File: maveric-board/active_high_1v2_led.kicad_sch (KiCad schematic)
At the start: 4 parts, among them Q1 DMN2005K-7

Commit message: some few notes
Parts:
- R14: value R_US -> 100R; JLCPCB Part # (none) -> C25076
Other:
- note added: "Vgs, max = 0.9V @ Id = 100uA, Vds = Vgs Cin = 36pF"
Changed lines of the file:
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@@
+		)
+	)
+	(text "Vgs, max = 0.9V @ Id = 100uA, Vds = Vgs\nCin = 36pF"
+		(exclude_from_sim no)
+		(at 85.598 52.07 0)
+		(effects
+			(font
+				(size 1.27 1.27)
+			)
 		)
 	)
@@
 			)
 		)
-		(property "Value" "R_US"
+		(property "Value" "100R"
 			(at 48.26 31.7499 0)
 			(effects
@@
 			)
 		)
-		(property "Description" "Resistor, US symbol"
+		(property "Description" "0402WGF1000TCE"
 			(at 45.72 30.48 0)
 			(effects
+				(font
+					(size 1.27 1.27)
+				)
+				(hide yes)
+			)
+		)
+		(property "JLCPCB Part #" "C25076"
+			(at 45.72 30.48 0)
+			(effects

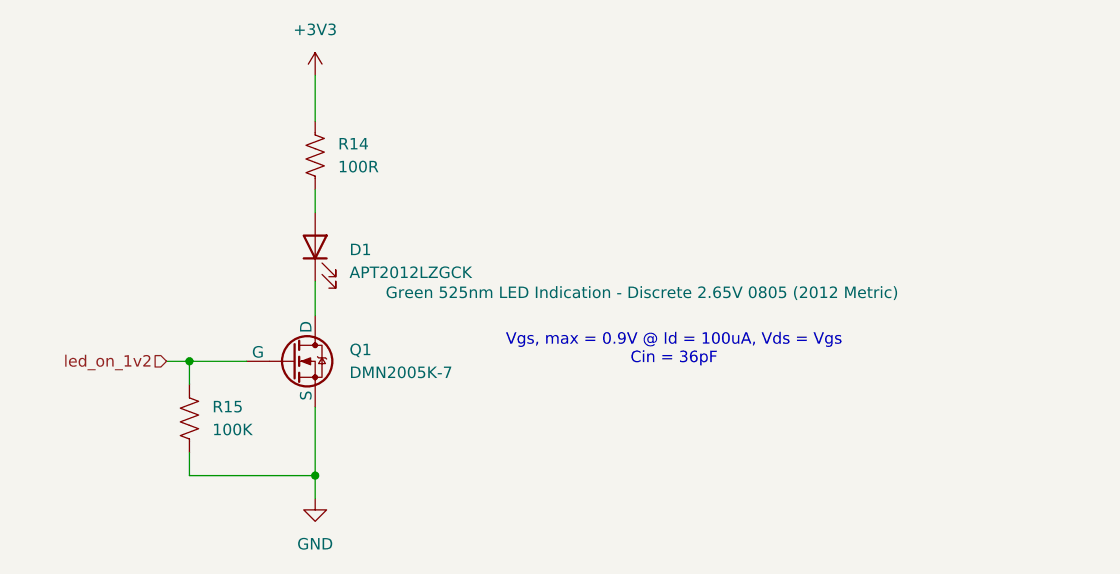
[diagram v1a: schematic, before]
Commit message: wire up the LEDs
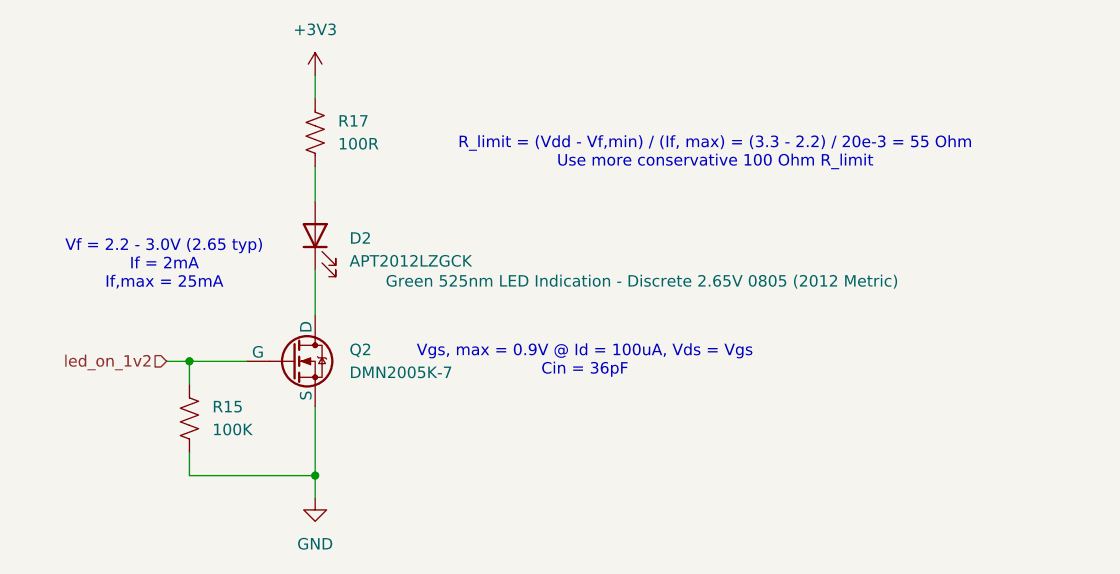
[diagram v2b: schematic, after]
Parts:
- renumbered D1 to D2, Q1 to Q2, R14 to R17
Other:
- note added: "R_limit = (Vdd - Vf,min) / (If, max) = (3.3 - 2.2) / 20e-3 = 55 Ohm Use more conservative 100 Ohm R_limit"
- note added: "Vf = 2.2 - 3.0V (2.65 typ) If = 2mA If,max = 25mA"
- moved on the sheet: D2, R17
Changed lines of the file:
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@@
-	(wire
-		(pts
-			(xy 45.72 34.29) (xy 45.72 36.83)
-		)
-		(stroke
-			(width 0)
-			(type default)
-		)
-	)
 	(wire
 		(pts
@@
 	(wire
 		(pts
-			(xy 45.72 44.45) (xy 45.72 48.26)
+			(xy 45.72 43.18) (xy 45.72 48.26)
 		)
 		(stroke
@@
 	(wire
 		(pts
-			(xy 45.72 21.59) (xy 45.72 26.67)
+			(xy 45.72 21.59) (xy 45.72 24.13)
+		)
+		(stroke
+			(width 0)
+			(type default)
+		)
+	)
+	(wire
+		(pts
+			(xy 45.72 31.75) (xy 45.72 35.56)
 		)
 		(stroke
@@
 		)
 	)
+	(text "Vf = 2.2 - 3.0V (2.65 typ)\nIf = 2mA\nIf,max = 25mA"
+		(exclude_from_sim no)
+		(at 28.956 42.672 0)
+		(effects
+			(font
+				(size 1.27 1.27)
+			)
+		)
+	)
+	(text "R_limit = (Vdd - Vf,min) / (If, max) = (3.3 - 2.2) / 20e-3 = 55 Ohm\nUse more conservative 100 Ohm R_limit"
+		(exclude_from_sim no)
+		(at 90.17 30.226 0)
+		(effects
+			(font
+				(size 1.27 1.27)
+			)
+		)
+	)
 	(text "Vgs, max = 0.9V @ Id = 100uA, Vds = Vgs\nCin = 36pF"
 		(exclude_from_sim no)
-		(at 85.598 52.07 0)
+		(at 75.692 53.34 0)
 		(effects
 			(font
@@
 		(dnp no)
 		(fields_autoplaced yes)
-		(property "Reference" "#PWR068"
+		(property "Reference" "#PWR091"
 			(at 45.72 74.93 0)
 			(effects
@@
 		)
 		(instances
-			(project ""
+			(project "maveric-board"
+				(path "/ae861d46-65fb-4872-932f-ad48addb0154/04d5a329-5af7-4fa0-b263-ed8b9ef94f0b"
+					(reference "#PWR091")
+					(unit 1)
+				)
+				(path "/ae861d46-65fb-4872-932f-ad48addb0154/07de628d-3b41-4acd-98a7-6b7c73c5b4dd"
+					(reference "#PWR093")
+					(unit 1)
+				)
+				(path "/ae861d46-65fb-4872-932f-ad48addb0154/482467b2-b94e-4ec7-a3c4-312d002b6711"
+					(reference "#PWR095")
+					(unit 1)
+				)
 				(path "/ae861d46-65fb-4872-932f-ad48addb0154/9dce5c8c-15df-41df-971c-7c9355dface0"
 					(reference "#PWR068")
+					(unit 1)
+				)
+				(path "/ae861d46-65fb-4872-932f-ad48addb0154/d720b503-5d41-4e8c-a69b-3a22cbc341eb"
+					(reference "#PWR097")
 					(unit 1)
 				)
@@
 		(dnp no)
 		(fields_autoplaced yes)
-		(property "Reference" "Q1"
+		(property "Reference" "Q2"
 			(at 49.53 52.0699 0)
 			(effects
@@
 		)
 		(instances
-			(project ""
-				(path "/ae861d46-65fb-4872-932f-ad48addb0154/9dce5c8c-15df-41df-971c-7c9355dface0"
-					(reference "Q1")
+			(project "maveric-board"
+				(path "/ae861d46-65fb-4872-932f-ad48addb0154/04d5a329-5af7-4fa0-b263-ed8b9ef94f0b"
+					(reference "Q2")
+					(unit 1)
+				)
+				(path "/ae861d46-65fb-4872-932f-ad48addb0154/07de628d-3b41-4acd-98a7-6b7c73c5b4dd"
+					(reference "Q3")
+					(unit 1)
+				)
+				(path "/ae861d46-65fb-4872-932f-ad48addb0154/482467b2-b94e-4ec7-a3c4-312d002b6711"
+					(reference "Q4")
+					(unit 1)
+				)
+				(path "/ae861d46-65fb-4872-932f-ad48addb0154/d720b503-5d41-4e8c-a69b-3a22cbc341eb"
+					(reference "Q5")
 					(unit 1)
 				)
@@
 	(symbol
 		(lib_id "Device:R_US")
-		(at 45.72 30.48 0)
+		(at 45.72 27.94 0)
 		(unit 1)
 		(exclude_from_sim no)
@@
 		(dnp no)
 		(fields_autoplaced yes)
-		(property "Reference" "R14"
+		(property "Reference" "R17"
+			(at 48.26 26.6699 0)
+			(effects
+				(font
+					(size 1.27 1.27)
+				)
+				(justify left)
+			)
+		)
+		(property "Value" "100R"
 			(at 48.26 29.2099 0)
 			(effects
@@
 			)
 		)
-		(property "Value" "100R"
-			(at 48.26 31.7499 0)
-			(effects
-				(font
-					(size 1.27 1.27)
-				)
-				(justify left)
-			)
-		)
 		(property "Footprint" ""
-			(at 46.736 30.734 90)
+			(at 46.736 28.194 90)
 			(effects
 				(font
@@
 		)
 		(property "Datasheet" "~"
-			(at 45.72 30.48 0)
+			(at 45.72 27.94 0)
 			(effects
 				(font
@@
 		)
 		(property "Description" "0402WGF1000TCE"
-			(at 45.72 30.48 0)
+			(at 45.72 27.94 0)
 			(effects
 				(font
@@
 		)
 		(property "JLCPCB Part #" "C25076"
-			(at 45.72 30.48 0)
+			(at 45.72 27.94 0)
 			(effects
 				(font
@@
 		)
 		(instances
-			(project ""
-				(path "/ae861d46-65fb-4872-932f-ad48addb0154/9dce5c8c-15df-41df-971c-7c9355dface0"
-					(reference "R14")
+			(project "maveric-board"
+				(path "/ae861d46-65fb-4872-932f-ad48addb0154/04d5a329-5af7-4fa0-b263-ed8b9ef94f0b"
+					(reference "R17")
+					(unit 1)
+				)
+				(path "/ae861d46-65fb-4872-932f-ad48addb0154/07de628d-3b41-4acd-98a7-6b7c73c5b4dd"
+					(reference "R19")
+					(unit 1)
+				)
+				(path "/ae861d46-65fb-4872-932f-ad48addb0154/482467b2-b94e-4ec7-a3c4-312d002b6711"
+					(reference "R21")
+					(unit 1)
+				)
+				(path "/ae861d46-65fb-4872-932f-ad48addb0154/d720b503-5d41-4e8c-a69b-3a22cbc341eb"
+					(reference "R23")
 					(unit 1)
 				)
@@
 		(instances
 			(project "maveric-board"
+				(path "/ae861d46-65fb-4872-932f-ad48addb0154/04d5a329-5af7-4fa0-b263-ed8b9ef94f0b"
+					(reference "R16")
+					(unit 1)
+				)
+				(path "/ae861d46-65fb-4872-932f-ad48addb0154/07de628d-3b41-4acd-98a7-6b7c73c5b4dd"
+					(reference "R18")
+					(unit 1)
+				)
+				(path "/ae861d46-65fb-4872-932f-ad48addb0154/482467b2-b94e-4ec7-a3c4-312d002b6711"
+					(reference "R20")
+					(unit 1)
+				)
 				(path "/ae861d46-65fb-4872-932f-ad48addb0154/9dce5c8c-15df-41df-971c-7c9355dface0"
 					(reference "R15")
 					(unit 1)
 				)
+				(path "/ae861d46-65fb-4872-932f-ad48addb0154/d720b503-5d41-4e8c-a69b-3a22cbc341eb"
+					(reference "R22")
+					(unit 1)
+				)
 			)
 		)
@@
 	(symbol
 		(lib_id "Device:LED")
-		(at 45.72 40.64 90)
+		(at 45.72 39.37 90)
 		(unit 1)
 		(exclude_from_sim no)
@@
 		(on_board yes)
 		(dnp no)
-		(property "Reference" "D1"
-			(at 49.53 40.9574 90)
+		(property "Reference" "D2"
+			(at 49.53 39.6874 90)
 			(effects
 				(font
@@
 		)
 		(property "Value" "APT2012LZGCK"
-			(at 49.53 43.4974 90)
+			(at 49.53 42.2274 90)
 			(effects
 				(font
@@
 		)
 		(property "Footprint" "maveric-parts:APT2012LZGCK"
-			(at 45.72 40.64 0)
+			(at 45.72 39.37 0)
 			(effects
 				(font
@@
 		)
 		(property "Datasheet" "~"
-			(at 45.72 40.64 0)
+			(at 45.72 39.37 0)
 			(effects
 				(font
@@
 		)
 		(property "Description" "Green 525nm LED Indication - Discrete 2.65V 0805 (2012 Metric)"
-			(at 82.042 45.72 90)
+			(at 82.042 44.45 90)
 			(effects
 				(font
@@
 		)
 		(property "JLCPCB Part #" "C5569446"
-			(at 45.72 40.64 90)
+			(at 45.72 39.37 90)
 			(effects
 				(font
@@
 		)
 		(instances
-			(project ""
-				(path "/ae861d46-65fb-4872-932f-ad48addb0154/9dce5c8c-15df-41df-971c-7c9355dface0"
-					(reference "D1")
+			(project "maveric-board"
+				(path "/ae861d46-65fb-4872-932f-ad48addb0154/04d5a329-5af7-4fa0-b263-ed8b9ef94f0b"
+					(reference "D2")
+					(unit 1)
+				)
+				(path "/ae861d46-65fb-4872-932f-ad48addb0154/07de628d-3b41-4acd-98a7-6b7c73c5b4dd"
+					(reference "D3")
+					(unit 1)
+				)
+				(path "/ae861d46-65fb-4872-932f-ad48addb0154/482467b2-b94e-4ec7-a3c4-312d002b6711"
+					(reference "D4")
+					(unit 1)
+				)
+				(path "/ae861d46-65fb-4872-932f-ad48addb0154/d720b503-5d41-4e8c-a69b-3a22cbc341eb"
+					(reference "D5")
 					(unit 1)
 				)
@@
 		(dnp no)
 		(fields_autoplaced yes)
-		(property "Reference" "#PWR066"
+		(property "Reference" "#PWR069"
 			(at 45.72 25.4 0)
 			(effects
@@
 		)
 		(instances
-			(project ""
+			(project "maveric-board"
+				(path "/ae861d46-65fb-4872-932f-ad48addb0154/04d5a329-5af7-4fa0-b263-ed8b9ef94f0b"
+					(reference "#PWR069")
+					(unit 1)
+				)
+				(path "/ae861d46-65fb-4872-932f-ad48addb0154/07de628d-3b41-4acd-98a7-6b7c73c5b4dd"
+					(reference "#PWR092")
+					(unit 1)
+				)
+				(path "/ae861d46-65fb-4872-932f-ad48addb0154/482467b2-b94e-4ec7-a3c4-312d002b6711"
+					(reference "#PWR094")
+					(unit 1)
+				)
 				(path "/ae861d46-65fb-4872-932f-ad48addb0154/9dce5c8c-15df-41df-971c-7c9355dface0"
 					(reference "#PWR066")
 					(unit 1)
 				)
+				(path "/ae861d46-65fb-4872-932f-ad48addb0154/d720b503-5d41-4e8c-a69b-3a22cbc341eb"
+					(reference "#PWR096")
+					(unit 1)
+				)

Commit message: add clocking notes
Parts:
- renumbered R15 to R16
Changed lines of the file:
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@@
 		(dnp no)
 		(fields_autoplaced yes)
-		(property "Reference" "R15"
+		(property "Reference" "R16"
 			(at 34.29 58.4199 0)
 			(effects

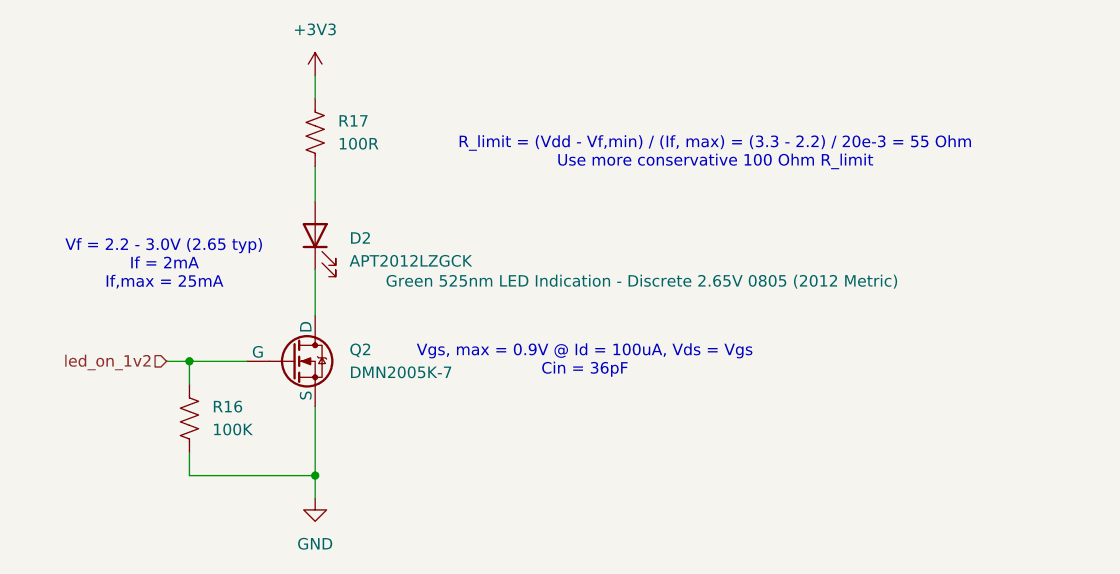
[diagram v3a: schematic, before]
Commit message: reannotate, fix all ERCs
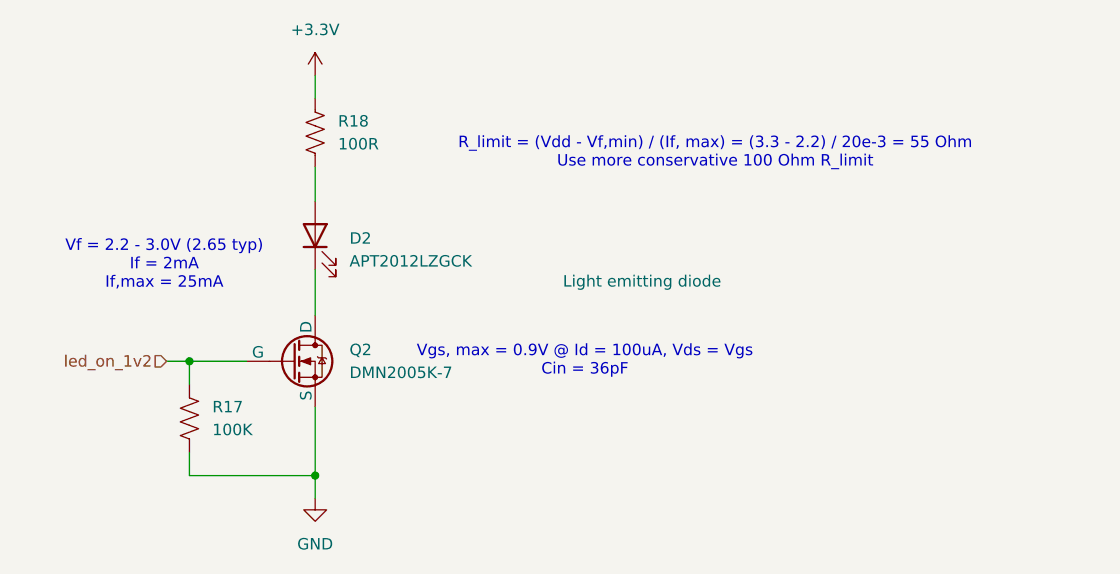
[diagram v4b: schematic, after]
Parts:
- renumbered R16 to R17, R17 to R18
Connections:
- net +3V3 renamed +3.3V
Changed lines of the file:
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@@
 		(dnp no)
 		(fields_autoplaced yes)
-		(property "Reference" "#PWR091"
+		(property "Reference" "#PWR095"
 			(at 45.72 74.93 0)
 			(effects
@@
 			(project "maveric-board"
 				(path "/ae861d46-65fb-4872-932f-ad48addb0154/04d5a329-5af7-4fa0-b263-ed8b9ef94f0b"
-					(reference "#PWR091")
+					(reference "#PWR095")
 					(unit 1)
 				)
 				(path "/ae861d46-65fb-4872-932f-ad48addb0154/07de628d-3b41-4acd-98a7-6b7c73c5b4dd"
+					(reference "#PWR097")
+					(unit 1)
+				)
+				(path "/ae861d46-65fb-4872-932f-ad48addb0154/482467b2-b94e-4ec7-a3c4-312d002b6711"
+					(reference "#PWR099")
+					(unit 1)
+				)
+				(path "/ae861d46-65fb-4872-932f-ad48addb0154/9dce5c8c-15df-41df-971c-7c9355dface0"
 					(reference "#PWR093")
 					(unit 1)
 				)
-				(path "/ae861d46-65fb-4872-932f-ad48addb0154/482467b2-b94e-4ec7-a3c4-312d002b6711"
-					(reference "#PWR095")
-					(unit 1)
-				)
-				(path "/ae861d46-65fb-4872-932f-ad48addb0154/9dce5c8c-15df-41df-971c-7c9355dface0"
-					(reference "#PWR068")
-					(unit 1)
-				)
 				(path "/ae861d46-65fb-4872-932f-ad48addb0154/d720b503-5d41-4e8c-a69b-3a22cbc341eb"
-					(reference "#PWR097")
+					(reference "#PWR0101")
 					(unit 1)
 				)
@@
 			)
 		)
-		(property "Datasheet" ""
+		(property "Datasheet" "https://ngspice.sourceforge.io/docs/ngspice-html-manual/manual.xhtml#cha_MOSFETs"
 			(at 43.18 66.04 0)
 			(effects
@@
 			)
 		)
-		(property "Description" "MOSFET N-CH 20V 300MA SOT23-3"
+		(property "Description" "N-MOSFET transistor, drain/source/gate"
 			(at 43.18 53.34 0)
 			(effects
@@
 		(property "JLCPCB Part #" "C260950"
 			(at 43.18 53.34 0)
+			(effects
+				(font
+					(size 1.27 1.27)
+				)
+				(hide yes)
+			)
+		)
+		(property "Sim.Device" "NMOS"
+			(at 43.18 70.485 0)
+			(effects
+				(font
+					(size 1.27 1.27)
+				)
+				(hide yes)
+			)
+		)
+		(property "Sim.Type" "VDMOS"
+			(at 43.18 72.39 0)
+			(effects
+				(font
+					(size 1.27 1.27)
+				)
+				(hide yes)
+			)
+		)
+		(property "Sim.Pins" "1=D 2=G 3=S"
+			(at 43.18 68.58 0)
 			(effects
 				(font
@@
 				(path "/ae861d46-65fb-4872-932f-ad48addb0154/482467b2-b94e-4ec7-a3c4-312d002b6711"
 					(reference "Q4")
+					(unit 1)
+				)
+				(path "/ae861d46-65fb-4872-932f-ad48addb0154/9dce5c8c-15df-41df-971c-7c9355dface0"
+					(reference "Q1")
 					(unit 1)
 				)
@@
 		(dnp no)
 		(fields_autoplaced yes)
-		(property "Reference" "R17"
+		(property "Reference" "R18"
 			(at 48.26 26.6699 0)
 			(effects
@@
 			)
 		)
-		(property "Description" "0402WGF1000TCE"
+		(property "Description" "Resistor, US symbol"
 			(at 45.72 27.94 0)
 			(effects
@@
 			(project "maveric-board"
 				(path "/ae861d46-65fb-4872-932f-ad48addb0154/04d5a329-5af7-4fa0-b263-ed8b9ef94f0b"
-					(reference "R17")
+					(reference "R18")
 					(unit 1)
 				)
 				(path "/ae861d46-65fb-4872-932f-ad48addb0154/07de628d-3b41-4acd-98a7-6b7c73c5b4dd"
-					(reference "R19")
+					(reference "R20")
 					(unit 1)
 				)
 				(path "/ae861d46-65fb-4872-932f-ad48addb0154/482467b2-b94e-4ec7-a3c4-312d002b6711"
-					(reference "R21")
+					(reference "R22")
+					(unit 1)
+				)
+				(path "/ae861d46-65fb-4872-932f-ad48addb0154/9dce5c8c-15df-41df-971c-7c9355dface0"
+					(reference "R16")
 					(unit 1)
 				)
 				(path "/ae861d46-65fb-4872-932f-ad48addb0154/d720b503-5d41-4e8c-a69b-3a22cbc341eb"
-					(reference "R23")
+					(reference "R24")
+					(unit 1)
+				)
+			)
+		)
+	)
+	(symbol
+		(lib_id "power:+3.3V")
+		(at 45.72 21.59 0)
+		(unit 1)
+		(exclude_from_sim no)
+		(in_bom yes)
+		(on_board yes)
+		(dnp no)
+		(fields_autoplaced yes)
+		(property "Reference" "#PWR092"
+			(at 45.72 25.4 0)
+			(effects
+				(font
+					(size 1.27 1.27)
+				)
+				(hide yes)
+			)
+		)
+		(property "Value" "+3.3V"
+			(at 45.72 16.51 0)
+			(effects
+				(font
+					(size 1.27 1.27)
+				)
+			)
+		)
+		(property "Footprint" ""
+			(at 45.72 21.59 0)
+			(effects
+				(font
+					(size 1.27 1.27)
+				)
+				(hide yes)
+			)
+		)
+		(property "Datasheet" ""
+			(at 45.72 21.59 0)
+			(effects
+				(font
+					(size 1.27 1.27)
+				)
+				(hide yes)
+			)
+		)
+		(property "Description" "Power symbol creates a global label with name \"+3.3V\""
+			(at 45.72 21.59 0)
+			(effects
+				(font
+					(size 1.27 1.27)
+				)
+				(hide yes)
+			)
+		)
+		(pin "1"
+		)
+		(instances
+			(project ""
+				(path "/ae861d46-65fb-4872-932f-ad48addb0154/04d5a329-5af7-4fa0-b263-ed8b9ef94f0b"
+					(reference "#PWR092")
+					(unit 1)
+				)
+				(path "/ae861d46-65fb-4872-932f-ad48addb0154/07de628d-3b41-4acd-98a7-6b7c73c5b4dd"
+					(reference "#PWR094")
+					(unit 1)
+				)
+				(path "/ae861d46-65fb-4872-932f-ad48addb0154/482467b2-b94e-4ec7-a3c4-312d002b6711"
+					(reference "#PWR096")
+					(unit 1)
+				)
+				(path "/ae861d46-65fb-4872-932f-ad48addb0154/9dce5c8c-15df-41df-971c-7c9355dface0"
+					(reference "#PWR023")
+					(unit 1)
+				)
+				(path "/ae861d46-65fb-4872-932f-ad48addb0154/d720b503-5d41-4e8c-a69b-3a22cbc341eb"
+					(reference "#PWR098")
 					(unit 1)
 				)
@@
 		(dnp no)
 		(fields_autoplaced yes)
-		(property "Reference" "R16"
+		(property "Reference" "R17"
 			(at 34.29 58.4199 0)
 			(effects
@@
 			)
 		)
-		(property "Description" "0603WAF1003T5E"
+		(property "Description" "Resistor, US symbol"
 			(at 31.75 59.69 0)
 			(effects
@@
 			(project "maveric-board"
 				(path "/ae861d46-65fb-4872-932f-ad48addb0154/04d5a329-5af7-4fa0-b263-ed8b9ef94f0b"
-					(reference "R16")
+					(reference "R17")
 					(unit 1)
 				)
 				(path "/ae861d46-65fb-4872-932f-ad48addb0154/07de628d-3b41-4acd-98a7-6b7c73c5b4dd"
-					(reference "R18")
+					(reference "R19")
 					(unit 1)
 				)
 				(path "/ae861d46-65fb-4872-932f-ad48addb0154/482467b2-b94e-4ec7-a3c4-312d002b6711"
-					(reference "R20")
+					(reference "R21")
 					(unit 1)
 				)
@@
 				)
 				(path "/ae861d46-65fb-4872-932f-ad48addb0154/d720b503-5d41-4e8c-a69b-3a22cbc341eb"
-					(reference "R22")
+					(reference "R23")
 					(unit 1)
 				)
@@
 			)
 		)
-		(property "Description" "Green 525nm LED Indication - Discrete 2.65V 0805 (2012 Metric)"
+		(property "Description" "Light emitting diode"
 			(at 82.042 44.45 90)
 			(effects
@@
 					(unit 1)
 				)
+				(path "/ae861d46-65fb-4872-932f-ad48addb0154/9dce5c8c-15df-41df-971c-7c9355dface0"
+					(reference "D1")
+					(unit 1)
+				)
 				(path "/ae861d46-65fb-4872-932f-ad48addb0154/d720b503-5d41-4e8c-a69b-3a22cbc341eb"
 					(reference "D5")
 					(unit 1)
 				)
-			)
-		)
-	)
-	(symbol
-		(lib_id "power:+3V3")
-		(at 45.72 21.59 0)
-		(unit 1)
-		(exclude_from_sim no)
-		(in_bom yes)
-		(on_board yes)
-		(dnp no)
-		(fields_autoplaced yes)
-		(property "Reference" "#PWR069"
-			(at 45.72 25.4 0)
-			(effects
-				(font
-					(size 1.27 1.27)
-				)
-				(hide yes)
-			)
-		)
-		(property "Value" "+3V3"
-			(at 45.72 16.51 0)
-			(effects
-				(font
-					(size 1.27 1.27)
-				)
-			)
-		)
-		(property "Footprint" ""
-			(at 45.72 21.59 0)
-			(effects
-				(font
-					(size 1.27 1.27)
-				)
-				(hide yes)
-			)
-		)
-		(property "Datasheet" ""
-			(at 45.72 21.59 0)
-			(effects
-				(font
-					(size 1.27 1.27)
-				)
-				(hide yes)
-			)
-		)
-		(property "Description" "Power symbol creates a global label with name \"+3V3\""
-			(at 45.72 21.59 0)
-			(effects
-				(font
-					(size 1.27 1.27)
-				)
-				(hide yes)
-			)
-		)
-		(pin "1"
-		)
-		(instances
-			(project "maveric-board"
-				(path "/ae861d46-65fb-4872-932f-ad48addb0154/04d5a329-5af7-4fa0-b263-ed8b9ef94f0b"
-					(reference "#PWR069")
-					(unit 1)
-				)
-				(path "/ae861d46-65fb-4872-932f-ad48addb0154/07de628d-3b41-4acd-98a7-6b7c73c5b4dd"
-					(reference "#PWR092")
-					(unit 1)
-				)
-				(path "/ae861d46-65fb-4872-932f-ad48addb0154/482467b2-b94e-4ec7-a3c4-312d002b6711"
-					(reference "#PWR094")
-					(unit 1)
-				)
-				(path "/ae861d46-65fb-4872-932f-ad48addb0154/9dce5c8c-15df-41df-971c-7c9355dface0"
-					(reference "#PWR066")
-					(unit 1)
-				)
-				(path "/ae861d46-65fb-4872-932f-ad48addb0154/d720b503-5d41-4e8c-a69b-3a22cbc341eb"
-					(reference "#PWR096")
-					(unit 1)
-				)
